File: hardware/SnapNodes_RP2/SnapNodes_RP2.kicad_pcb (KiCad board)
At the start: 2 copper layers, 85 x 40 mm, 166 parts, among them J1 P_Female, J10 LCD, J11 USB_C, J12 P_Female_Fallback, J13 P_Male_Fallback, J14 P_Female_Fallback, J15 P_Male_Fallback, J16 P_Female_Fallback, J17 P_Male_Fallback, J18 P_Female_Fallback, J19 P_Male_Fallback, J2 P_Male, J20 Conn_01x24_MountingPin, J21 Conn_01x24_MountingPin, J3 P_Female, J4 P_Male, J5 P_Female, J6 P_Male, J7 P_Female, J8 P_Male, J9 SWD, Q1 2N7002W, SW1 Left, SW2 Left, SW3 Left, SW4 Left, SW5 Left, U1 RP2350_80QFN, U2 TPS62A01PDDC, U3 BQ24232RGT, U4 ESP-PSRAM64H, U6 PY25Q128HA-SSH, U7 74AHC1G04, U8 LSM6DS3, U9 AW9523B, Y1 12M

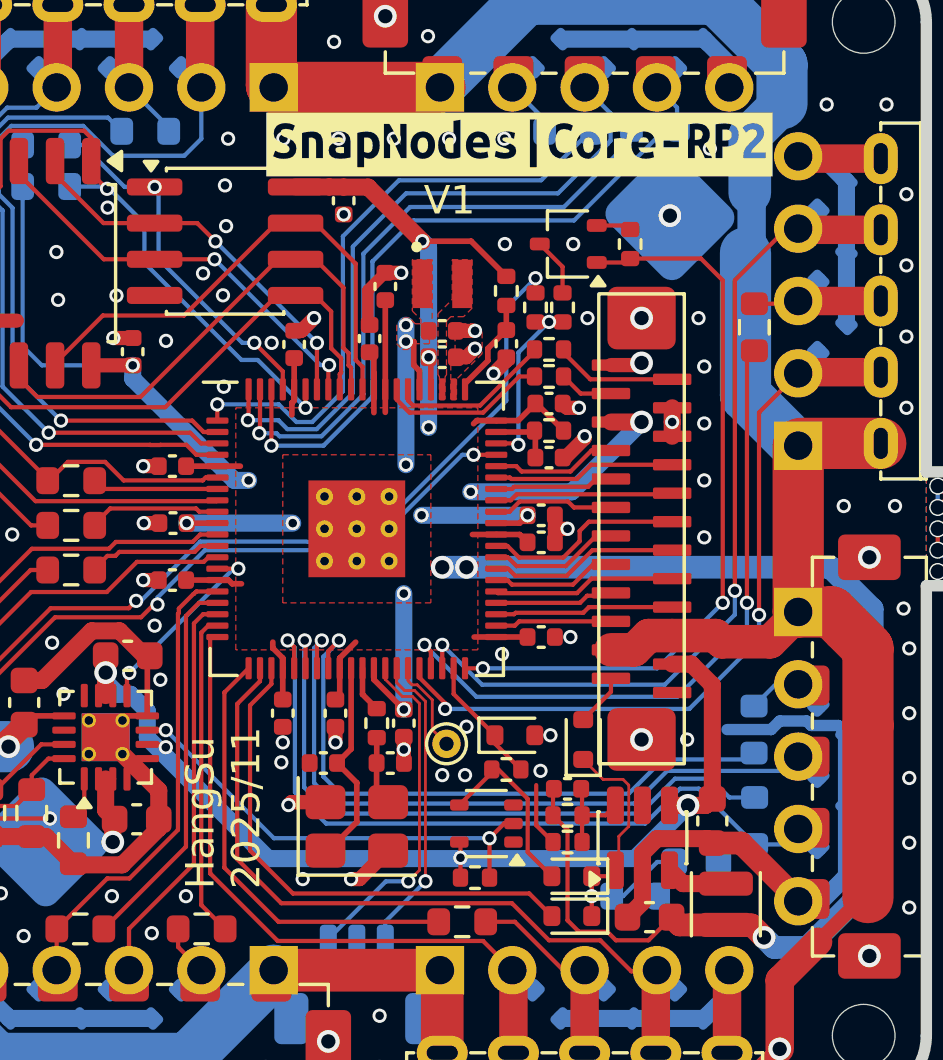
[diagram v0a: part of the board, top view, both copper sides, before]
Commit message: Rename PCB project to SnapNodes-RP2
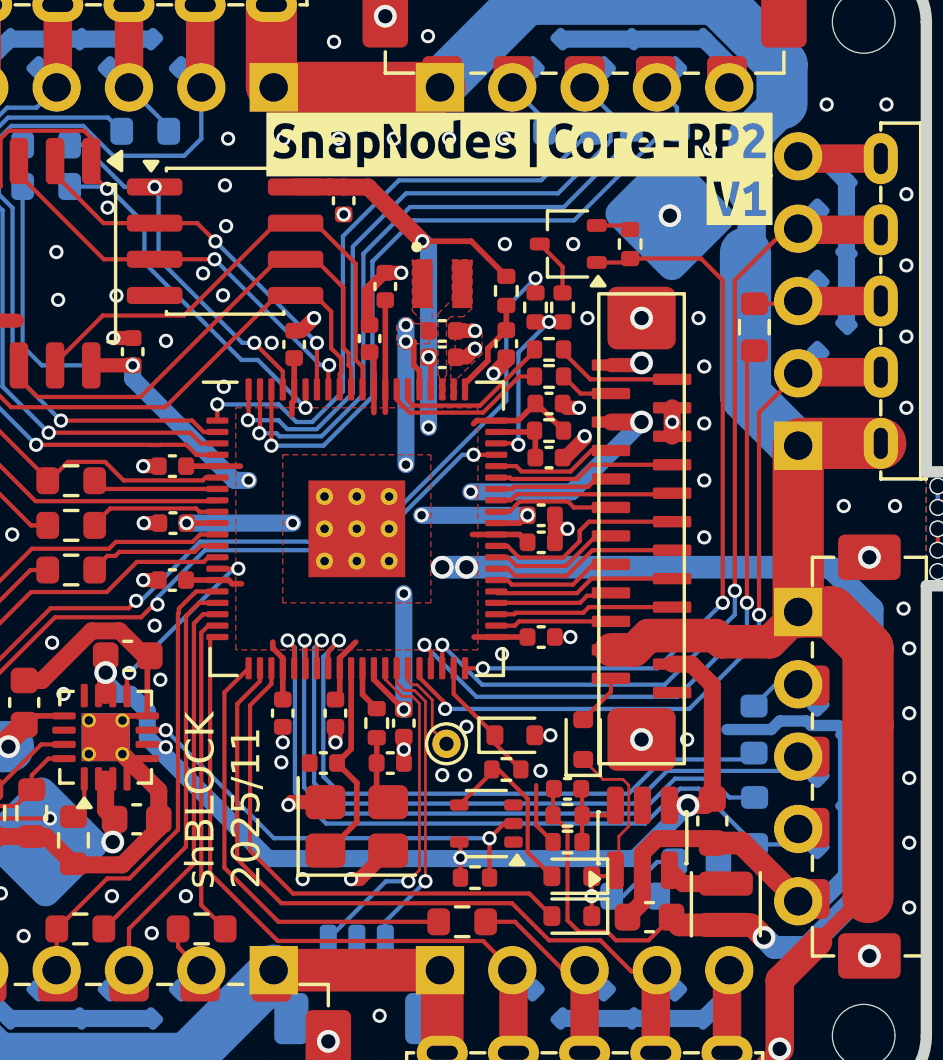
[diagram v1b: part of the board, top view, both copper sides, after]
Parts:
- added kibuzzard-6913C2AE: G***, kibuzzard-6913C2AE, F.Cu at (13.4, -11.6)
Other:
- board text added: "shBLOCK 2025/11"
- board text removed: "HangSu 2025/11"
- board text removed: "V1"
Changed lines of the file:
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@@
 		(property ki_fp_filters "Connector*:*_1x??-1MP*")
 		(sheetname "/")
-		(sheetfile "TileGlobeMC_Node.kicad_sch")
+		(sheetfile "SnapNodes_RP2.kicad_sch")
 		(attr smd)
 		(fp_rect
@@
 		)
 	)
+	(footprint "kibuzzard-6913C2AE"
+		(layer "F.Cu")
+		(at 13.4427 -11.55)
+		(descr "Generated with KiBuzzard")
+		(tags "kb_params=eyJBbGlnbm1lbnRDaG9pY2UiOiAiQ2VudGVyIiwgIkNhcExlZnRDaG9pY2UiOiAiWyIsICJDYXBSaWdodENob2ljZSI6ICJdIiwgIkZvbnRDb21ib0JveCI6ICJVYnVudHVNb25vLUIiLCAiSGVpZ2h0Q3RybCI6IDEuMiwgIkxheWVyQ29tYm9Cb3giOiAiRi5TaWxrUyIsICJMaW5lU3BhY2luZ0N0cmwiOiAxLjAsICJNdWx0aUxpbmVUZXh0IjogIlYxIiwgIlBhZGRpbmdCb3R0b21DdHJsIjogMi4wLCAiUGFkZGluZ0xlZnRDdHJsIjogMS41LCAiUGFkZGluZ1JpZ2h0Q3RybCI6IDEuNSwgIlBhZGRpbmdUb3BDdHJsIjogMS41LCAiV2lkdGhDdHJsIjogMC4wLCAiYWR2YW5jZWRDaGVja2JveCI6IHRydWUsICJpbmxpbmVGb3JtYXRUZXh0Ym94IjogZmFsc2UsICJsaW5lb3ZlclN0eWxlQ2hvaWNlIjogIlNxdWFyZSIsICJsaW5lb3ZlclRoaWNrbmVzc0N0cmwiOiAxfQ==")
+		(property "Reference" "kibuzzard-6913C2AE"
+			(at 0 -3.930714 0)
+			(layer "F.SilkS")
+			(hide yes)
+			(effects
+				(font
+					(size 0.001 0.001)
+				)
+			)
+		)
+		(property "Value" "G***"
+			(at 0 3.930714 0)
+			(layer "F.SilkS")
+			(hide yes)
+			(effects
+				(font
+					(size 0.001 0.001)
+				)
+			)
+		)
+		(property "Datasheet" ""
+			(at 0 0 0)
+			(layer "F.Fab")
+			(hide yes)
+			(effects
+				(font
+					(size 1.27 1.27)
+					(thickness 0.15)
+				)
+			)
+		)
+		(property "Description" ""
+			(at 0 0 0)
+			(layer "F.Fab")
+			(hide yes)
+			(effects
+				(font
+					(size 1.27 1.27)
+					(thickness 0.15)
+				)
+			)
+		)
+		(attr board_only exclude_from_pos_files exclude_from_bom)
+		(fp_poly
+			(pts
+				(xy -0.916963 -0.882714) (xy -1.159289 -0.882714) (xy -1.159289 0.882714) (xy -0.916963 0.882714)
+				(xy -0.581583 0.882714) (xy -0.581583 0.559612) (xy -0.629564 0.417124) (xy -0.680452 0.257189)
+				(xy -0.714701 0.144857) (xy -0.747658 0.032741) (xy -0.779321 -0.07916) (xy -0.809262 -0.188907)
+				(xy -0.837049 -0.294561) (xy -0.862682 -0.396123) (xy -0.894669 -0.531826) (xy -0.916963 -0.640388)
+				(xy -0.664943 -0.640388) (xy -0.650404 -0.539822) (xy -0.630048 -0.424233) (xy -0.605574 -0.299192)
+				(xy -0.578675 -0.170275) (xy -0.549596 -0.040388) (xy -0.518578 0.087561) (xy -0.486834 0.207997)
+				(xy -0.455574 0.315347) (xy -0.424556 0.209451) (xy -0.393538 0.089499) (xy -0.363489 -0.038449)
+				(xy -0.33538 -0.168336) (xy -0.309208 -0.297496) (xy -0.284976 -0.423263) (xy -0.263651 -0.53958)
+				(xy -0.246204 -0.640388) (xy 0.003877 -0.640388) (xy -0.022052 -0.517286) (xy -0.053312 -0.380614)
+				(xy -0.089661 -0.233522) (xy -0.130856 -0.07916) (xy -0.160905 0.026817) (xy -0.192892 0.134087)
+				(xy -0.226817 0.242649) (xy -0.262143 0.350673) (xy -0.298331 0.456327) (xy -0.33538 0.559612) (xy -0.581583 0.559612)
+				(xy -0.581583 0.882714) (xy 0.916963 0.882714) (xy 0.916963 0.559612) (xy 0.188045 0.559612) (xy 0.188045 0.361874)
+				(xy 0.440065 0.361874) (xy 0.440065 -0.308885) (xy 0.315994 -0.240065) (xy 0.197738 -0.192569) (xy 0.120194 -0.390307)
+				(xy 0.221002 -0.434895) (xy 0.329564 -0.494992) (xy 0.43231 -0.564782) (xy 0.51567 -0.640388) (xy 0.678514 -0.640388)
+				(xy 0.678514 0.361874) (xy 0.916963 0.361874) (xy 0.916963 0.559612) (xy 0.916963 0.882714) (xy 1.159289 0.882714)
+				(xy 1.159289 -0.882714) (xy 0.916963 -0.882714) (xy -0.916963 -0.882714)
+			)
+			(stroke
+				(width 0)
+				(type solid)
+			)
+			(fill yes)
+			(layer "F.SilkS")
+		)
+		(embedded_fonts no)
+	)
 	(footprint "Project:VQFN-16-1EP_3x3mm_P0.5mm_EP1.68x1.68mm_ThermalVias"
 		(layer "F.Cu")
@@
 				(font
 					(size 0.001 0.001)
+					(thickness 0.15)
 				)
 			)
@@
 				(font
 					(size 0.001 0.001)
+					(thickness 0.15)
 				)
 			)
@@
 		(property ki_fp_filters "Connector*:*_1x??-1MP*")
 		(sheetname "/")
-		(sheetfile "TileGlobeMC_Node.kicad_sch")
+		(sheetfile "SnapNodes_RP2.kicad_sch")
 		(attr smd)
 		(fp_rect
@@
 		(layer "Edge.Cuts")
 	)
-	(gr_text "V1"
-		(at 2.35 -10.95 0)
-		(layer "F.SilkS")
-		(effects
-			(font
-				(size 1 1)
-				(thickness 0.15)
-			)
-			(justify left bottom)
-		)
-	)
-	(gr_text "HangSu\n2025/11"
+	(gr_text "shBLOCK\n2025/11"
 		(at -3.3 12.65 90)
 		(layer "F.SilkS")

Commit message: PCB minor changes
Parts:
- added kibuzzard-6913C792: G***, kibuzzard-6913C792, F.Cu at (35.2, -8.25)
- SW1: value Left -> Center
- SW3: value Left -> Bottom
- SW4: value Left -> Right
- SW5: value Left -> Top

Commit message: PCB minor changes
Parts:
- C30, C31, C32, C33, C34, C35, D3, JP3, JP4, JP5, R31, R35, R36, R37, R38, R39, R40, R41, R42, R43, R44, R45, U9, kibuzzard-6913C792: moved to B.Cu
- moved C32 13.5 mm to (53.2, 11.8), turned to 180 degrees
- moved R39 13.5 mm to (53.2, 10.3), turned to 0 degrees
- moved R42 13.5 mm to (53.2, 13.3), turned to 180 degrees
- moved JP3 7.31 mm to (34.8, 6.74), turned to 90 degrees
- moved JP4 7.31 mm to (37.3, 6.74), turned to 90 degrees
- moved JP5 7.31 mm to (39.8, 6.74), turned to 90 degrees
- moved U9 4.49 mm to (35.0, 11.8), turned to -90 degrees
- moved C35 1.97 mm to (31.6, 12.9)
- moved R36 0.70 mm to (38.2, 0.82)
- moved R37 0.70 mm to (39.8, 0.82)
- moved kibuzzard-6913C792 0.60 mm to (35.6, -8.70), turned to 180 degrees
- moved C30 0.60 mm to (46.1, -4.85)
- moved D3 0.60 mm to (43.2, -4.85)
- moved R35 0.60 mm to (47.6, -4.85)
- moved R45 0.60 mm to (44.6, -4.85)
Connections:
- U9 pad 10: BTN_BOTTOM -> BTN_LEFT
- U9 pad 12: BTN_LEFT -> BTN_BOTTOM
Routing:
- net BTN_BOTTOM: track 9.40 -> 24.8 mm, vias 0 -> 2
- net GND_PERI: track 75.2 -> 62.1 mm, vias 68 -> 70
- net BTN_TOP: track 23.8 -> 33.2 mm, vias 0 -> 2
- net BTN_LEFT: track 8.85 -> 14.8 mm, vias 0 -> 2
- net LCD_BL: track 20.0 -> 14.1 mm, vias 1 -> 0
- net /Peripheral/+3V3: track 135.3 -> 140.3 mm, vias 8 -> 5
- net /Peripheral/I2C_SCL: track 27.7 -> 32.5 mm, vias 3 -> 4
- net Net-(R39-Pad1): track 7.09 -> 10.7 mm, vias 0 -> 1
- net /Peripheral/PERI_INT: track 29.1 -> 25.6 mm, vias 1 -> 2
- net BTN_RIGHT: track 26.2 -> 23.4 mm, vias 0 -> 2
- net /Peripheral/I2C_SDA: track 26.3 -> 27.0 mm, vias 3 -> 4
- net LCD_RST: track 17.8 -> 17.1 mm, vias 3 -> 0
- net /Peripheral/BTN_CENTER_VBUS: track 18.4 -> 19.1 mm, vias 1 -> 2
- net /Peripheral/BTN_CENTER: track 8.91 -> 9.31 mm, vias 1 -> 0
- net IMU_INT1: track 15.0 -> 15.3 mm, vias 1 -> 2
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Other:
- outline, holes or cut-outs redrawn
